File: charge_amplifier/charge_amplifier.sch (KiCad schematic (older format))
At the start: 31 parts, among them J1 TEST_1P, J2 TEST_1P, J3 Conn_01x02, J4 Conn_01x02, J5 Conn_01x02, J6 TEST_1P, U1 TL072

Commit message: Initial draft of layout
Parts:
- AE1: footprint (none) -> lib_fp:BNC_5227677-1
- D1: footprint (none) -> Diodes_SMD:D_SOD-323
- J1, J2, J6: footprint (none) -> Measurement_Points:Measurement_Point_Round-SMD-Pad_Small
- NE1: footprint (none) -> lib_fp:A1D-T
- U1: footprint (none) -> SMD_Packages:SOIC-8-N
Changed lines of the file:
@@
 LIBS:contrib
 LIBS:valves
+LIBS:charge_amplifier-cache
 EELAYER 25 0
 EELAYER END
@@
 F 0 "AE1" H 1575 3575 50  0000 R CNN
 F 1 "Antenna_Shield" H 1575 3500 50  0001 R CNN
-F 2 "" H 1650 3500 50  0001 C CNN
+F 2 "lib_fp:BNC_5227677-1" H 1650 3500 50  0001 C CNN
 F 3 "" H 1650 3500 50  0001 C CNN
 	1    1650 3400
@@
 F 0 "NE1" H 1775 3975 50  0000 L CNN
 F 1 "Lamp_Neon" H 2000 3950 50  0001 L CNN
-F 2 "" V 1975 4200 50  0001 C CNN
+F 2 "lib_fp:A1D-T" V 1975 4200 50  0001 C CNN
 F 3 "" V 1975 4200 50  0001 C CNN
 F 4 "Visual Communications Company - VCC" H 1975 4100 60  0001 C CNN "MFG Name"
@@
 F 0 "U1" H 4750 3950 50  0000 L CNN
 F 1 "TL072" H 4750 3550 50  0000 L CNN
-F 2 "" H 4750 3750 50  0001 C CNN
+F 2 "SMD_Packages:SOIC-8-N" H 4750 3750 50  0001 C CNN
 F 3 "" H 4750 3750 50  0001 C CNN
 F 4 "Texas Instruments" H 4750 3750 60  0001 C CNN "MFG Name"
@@
 F 0 "U1" H 7600 3925 50  0000 L CNN
 F 1 "TL072" H 7600 3525 50  0000 L CNN
-F 2 "" H 7600 3725 50  0001 C CNN
+F 2 "SMD_Packages:SOIC-8-N" H 7600 3725 50  0001 C CNN
 F 3 "" H 7600 3725 50  0001 C CNN
 F 4 "Value" H 7600 3725 60  0001 C CNN "MFG Name"
@@
 F 0 "J1" H 3750 4120 50  0000 C CNN
 F 1 "TEST_1P" H 3750 4050 50  0000 C CNN
-F 2 "" H 3950 3850 50  0001 C CNN
+F 2 "Measurement_Points:Measurement_Point_Round-SMD-Pad_Small" H 3950 3850 50  0001 C CNN
 F 3 "" H 3950 3850 50  0001 C CNN
 	1    3750 3850
@@
 F 0 "J2" H 5725 3970 50  0000 C CNN
 F 1 "TEST_1P" H 5725 3900 50  0000 C CNN
-F 2 "" H 5925 3700 50  0001 C CNN
+F 2 "Measurement_Points:Measurement_Point_Round-SMD-Pad_Small" H 5925 3700 50  0001 C CNN
 F 3 "" H 5925 3700 50  0001 C CNN
 	1    5725 3700
@@
 F 0 "J6" H 8225 3970 50  0000 C CNN
 F 1 "TEST_1P" H 8225 3900 50  0000 C CNN
-F 2 "" H 8425 3700 50  0001 C CNN
+F 2 "Measurement_Points:Measurement_Point_Round-SMD-Pad_Small" H 8425 3700 50  0001 C CNN
 F 3 "" H 8425 3700 50  0001 C CNN
 	1    8225 3700
@@
 F 0 "D1" H 2525 4225 50  0000 C CNN
 F 1 "D_Schottky" H 2525 4025 50  0001 C CNN
-F 2 "" H 2525 4125 50  0001 C CNN
+F 2 "Diodes_SMD:D_SOD-323" H 2525 4125 50  0001 C CNN
 F 3 "" H 2525 4125 50  0001 C CNN
 	1    2525 4125

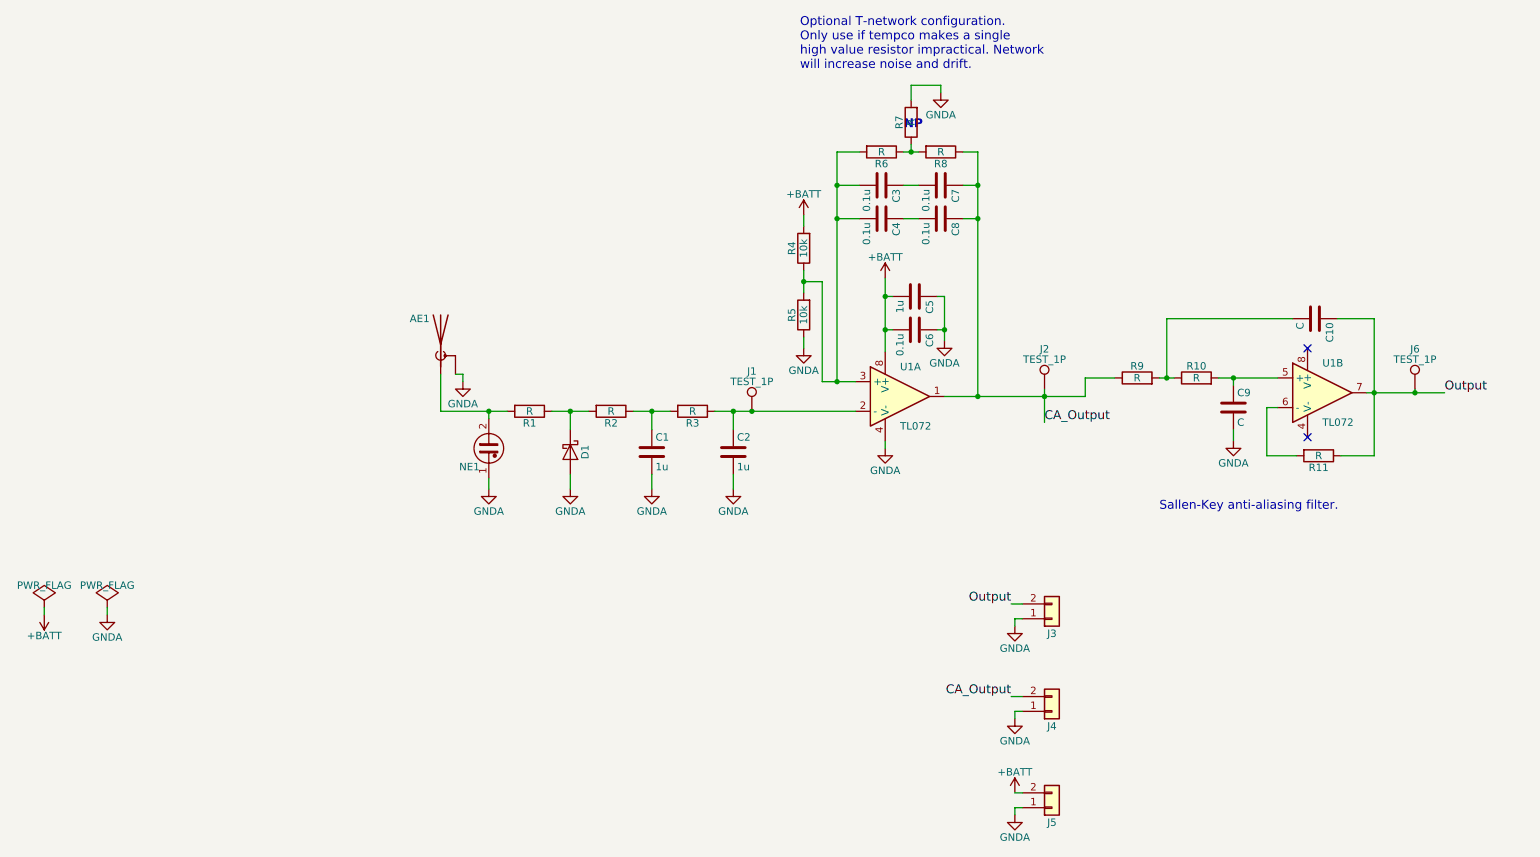
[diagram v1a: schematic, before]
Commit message: Fix schematic with bodges on Rev.A
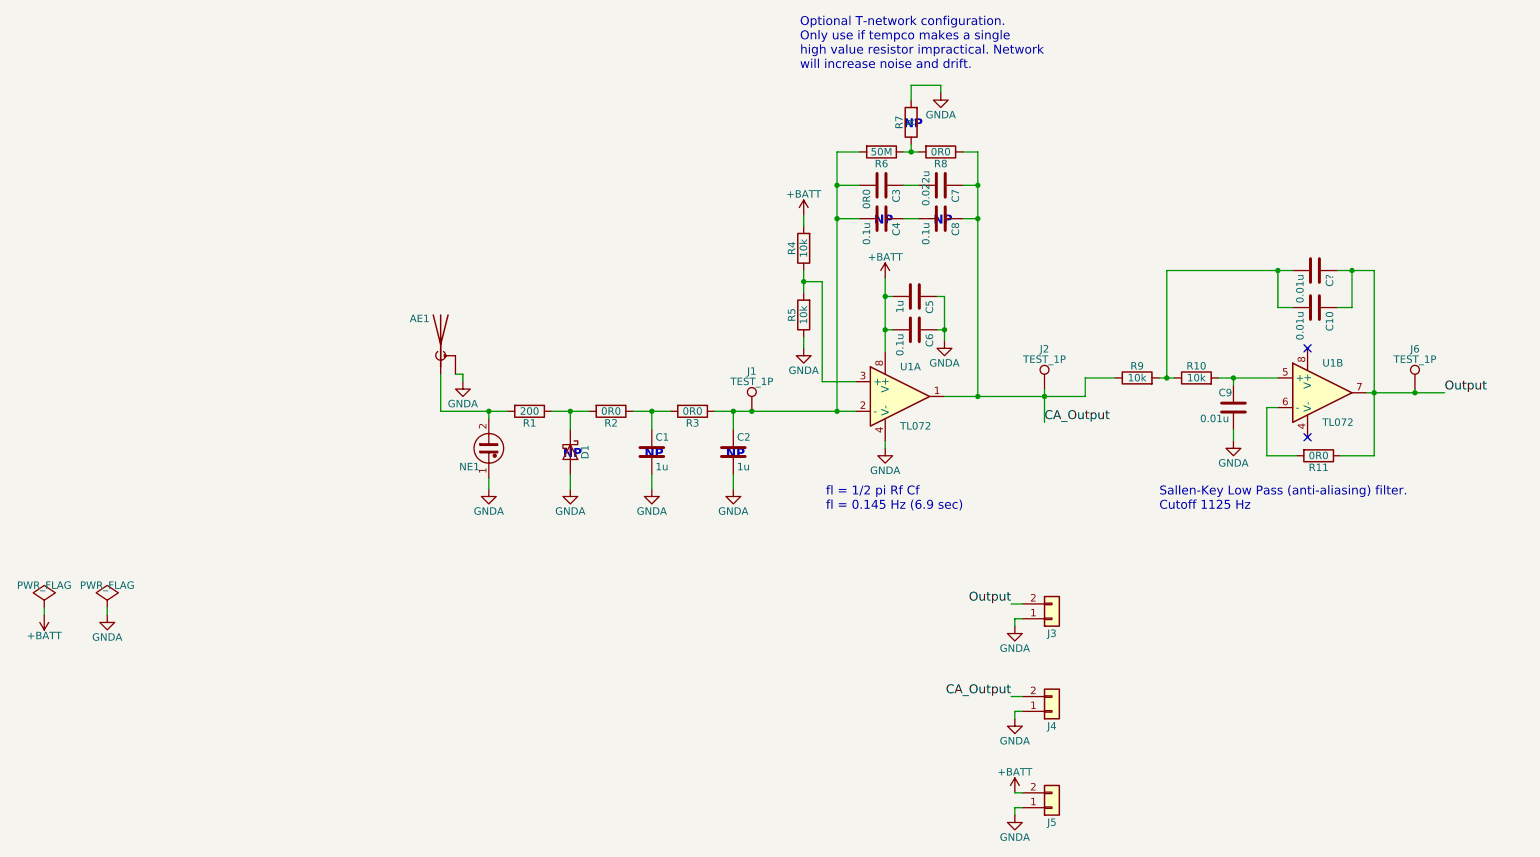
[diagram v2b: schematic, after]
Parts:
- added C?: 0.01u, Capacitors_SMD:C_0603_HandSoldering, symbol C
- C10, C9: value C -> 0.01u
- C3: value 0.1u -> 0R0
- C7: value 0.1u -> 0.022u
- R1: value R -> 200; 1st Distrib Link (none) -> Value; 1st Distrib PN (none) -> Value; 2nd Distrib Link (none) -> Value; 2nd Distrib PN (none) -> Value; MFG Name (none) -> Value; MFG Part Num (none) -> Value
- R10, R9: value R -> 10k
- R11, R2, R3, R8: value R -> 0R0; 1st Distrib Link (none) -> Value; 1st Distrib PN (none) -> Value; 2nd Distrib Link (none) -> Value; 2nd Distrib PN (none) -> Value; MFG Name (none) -> Value; MFG Part Num (none) -> Value
- R6: value R -> 50M; 1st Distrib Link (none) -> Value; 1st Distrib PN (none) -> Value; 2nd Distrib Link (none) -> Value; 2nd Distrib PN (none) -> Value; MFG Name (none) -> Value; MFG Part Num (none) -> Value
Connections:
- net Output: now also C?.1
- net at C2.1, J1.1, R3.1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: now also C3.2, C4.2, R6.2
- net at R4.1, R5.2, U1.3 (+): no longer C3.2, C4.2, R6.2
- net at C10.2, R10.1, R9.2: now also C?.2
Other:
- note added: "Sallen-Key Low Pass (anti-aliasing) filter.\nCutoff 1125 Hz"
- note added: "fl = 1/2 pi Rf Cf\nfl = 0.145 Hz (6.9 sec)"
- note removed: "Sallen-Key anti-aliasing filter."
- moved on the sheet: C10
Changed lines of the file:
@@
 P 2250 3850
 F 0 "R1" V 2330 3850 50  0000 C CNN
-F 1 "R" V 2250 3850 50  0000 C CNN
+F 1 "200" V 2250 3850 50  0000 C CNN
 F 2 "Resistors_SMD:R_0603_HandSoldering" V 2180 3850 50  0001 C CNN
 F 3 "" H 2250 3850 50  0001 C CNN
+F 4 "Value" H 2250 3850 60  0001 C CNN "MFG Name"
+F 5 "Value" H 2250 3850 60  0001 C CNN "MFG Part Num"
+F 6 "Value" H 2250 3850 60  0001 C CNN "1st Distrib PN"
+F 7 "Value" H 2250 3850 60  0001 C CNN "1st Distrib Link"
+F 8 "Value" H 2250 3850 60  0001 C CNN "2nd Distrib PN"
+F 9 "Value" H 2250 3850 60  0001 C CNN "2nd Distrib Link"
 	1    2250 3850
 	0    1    1    0
@@
 P 2800 3850
 F 0 "R2" V 2880 3850 50  0000 C CNN
-F 1 "R" V 2800 3850 50  0000 C CNN
+F 1 "0R0" V 2800 3850 50  0000 C CNN
 F 2 "Resistors_SMD:R_0603_HandSoldering" V 2730 3850 50  0001 C CNN
 F 3 "" H 2800 3850 50  0001 C CNN
+F 4 "Value" H 2800 3850 60  0001 C CNN "MFG Name"
+F 5 "Value" H 2800 3850 60  0001 C CNN "MFG Part Num"
+F 6 "Value" H 2800 3850 60  0001 C CNN "1st Distrib PN"
+F 7 "Value" H 2800 3850 60  0001 C CNN "1st Distrib Link"
+F 8 "Value" H 2800 3850 60  0001 C CNN "2nd Distrib PN"
+F 9 "Value" H 2800 3850 60  0001 C CNN "2nd Distrib Link"
 	1    2800 3850
 	0    1    1    0
@@
 P 3350 3850
 F 0 "R3" V 3430 3850 50  0000 C CNN
-F 1 "R" V 3350 3850 50  0000 C CNN
+F 1 "0R0" V 3350 3850 50  0000 C CNN
 F 2 "Resistors_SMD:R_0603_HandSoldering" V 3280 3850 50  0001 C CNN
 F 3 "" H 3350 3850 50  0001 C CNN
+F 4 "Value" H 3350 3850 60  0001 C CNN "MFG Name"
+F 5 "Value" H 3350 3850 60  0001 C CNN "MFG Part Num"
+F 6 "Value" H 3350 3850 60  0001 C CNN "1st Distrib PN"
+F 7 "Value" H 3350 3850 60  0001 C CNN "1st Distrib Link"
+F 8 "Value" H 3350 3850 60  0001 C CNN "2nd Distrib PN"
+F 9 "Value" H 3350 3850 60  0001 C CNN "2nd Distrib Link"
 	1    3350 3850
 	0    1    1    0
@@
 P 6350 3625
 F 0 "R9" V 6430 3625 50  0000 C CNN
-F 1 "R" V 6350 3625 50  0000 C CNN
+F 1 "10k" V 6350 3625 50  0000 C CNN
 F 2 "Resistors_SMD:R_0603_HandSoldering" V 6280 3625 50  0001 C CNN
 F 3 "" H 6350 3625 50  0001 C CNN
@@
 P 5025 2325
 F 0 "C7" H 5050 2425 50  0000 L CNN
-F 1 "0.1u" H 5050 2225 50  0000 L CNN
+F 1 "0.022u" H 4925 2225 50  0000 L CNN
 F 2 "Capacitors_SMD:C_0603_HandSoldering" H 5063 2175 50  0001 C CNN
 F 3 "" H 5025 2325 50  0001 C CNN
@@
 P 4625 2325
 F 0 "C3" H 4650 2425 50  0000 L CNN
-F 1 "0.1u" H 4650 2225 50  0000 L CNN
+F 1 "0R0" H 4650 2225 50  0000 L CNN
 F 2 "Capacitors_SMD:C_0603_HandSoldering" H 4663 2175 50  0001 C CNN
 F 3 "" H 4625 2325 50  0001 C CNN
@@
 P 4625 2100
 F 0 "R6" V 4705 2100 50  0000 C CNN
-F 1 "R" V 4625 2100 50  0000 C CNN
+F 1 "50M" V 4625 2100 50  0000 C CNN
 F 2 "Resistors_SMD:R_0603_HandSoldering" V 4555 2100 50  0001 C CNN
 F 3 "" H 4625 2100 50  0001 C CNN
+F 4 "Value" H 4625 2100 60  0001 C CNN "MFG Name"
+F 5 "Value" H 4625 2100 60  0001 C CNN "MFG Part Num"
+F 6 "Value" H 4625 2100 60  0001 C CNN "1st Distrib PN"
+F 7 "Value" H 4625 2100 60  0001 C CNN "1st Distrib Link"
+F 8 "Value" H 4625 2100 60  0001 C CNN "2nd Distrib PN"
+F 9 "Value" H 4625 2100 60  0001 C CNN "2nd Distrib Link"
 	1    4625 2100
 	0    1    1    0
@@
 P 5025 2100
 F 0 "R8" V 5105 2100 50  0000 C CNN
-F 1 "R" V 5025 2100 50  0000 C CNN
+F 1 "0R0" V 5025 2100 50  0000 C CNN
 F 2 "Resistors_SMD:R_0603_HandSoldering" V 4955 2100 50  0001 C CNN
 F 3 "" H 5025 2100 50  0001 C CNN
+F 4 "Value" H 5025 2100 60  0001 C CNN "MFG Name"
+F 5 "Value" H 5025 2100 60  0001 C CNN "MFG Part Num"
+F 6 "Value" H 5025 2100 60  0001 C CNN "1st Distrib PN"
+F 7 "Value" H 5025 2100 60  0001 C CNN "1st Distrib Link"
+F 8 "Value" H 5025 2100 60  0001 C CNN "2nd Distrib PN"
+F 9 "Value" H 5025 2100 60  0001 C CNN "2nd Distrib Link"
 	1    5025 2100
 	0    1    1    0
@@
 P 7575 4150
 F 0 "R11" V 7655 4150 50  0000 C CNN
-F 1 "R" V 7575 4150 50  0000 C CNN
+F 1 "0R0" V 7575 4150 50  0000 C CNN
 F 2 "Resistors_SMD:R_0603_HandSoldering" V 7505 4150 50  0001 C CNN
 F 3 "" H 7575 4150 50  0001 C CNN
+F 4 "Value" H 7575 4150 60  0001 C CNN "MFG Name"
+F 5 "Value" H 7575 4150 60  0001 C CNN "MFG Part Num"
+F 6 "Value" H 7575 4150 60  0001 C CNN "1st Distrib PN"
+F 7 "Value" H 7575 4150 60  0001 C CNN "1st Distrib Link"
+F 8 "Value" H 7575 4150 60  0001 C CNN "2nd Distrib PN"
+F 9 "Value" H 7575 4150 60  0001 C CNN "2nd Distrib Link"
 	1    7575 4150
 	0    1    1    0
@@
 Optional T-network configuration.\nOnly use if tempco makes a single\nhigh value resistor impractical. Network\nwill increase noise and drift.
 Text Notes 6500 4525 0    60   ~ 0
-Sallen-Key anti-aliasing filter.
+Sallen-Key Low Pass (anti-aliasing) filter.\nCutoff 1125 Hz
 $Comp
 L GNDA #PWR02
@@
 	4475 2100 4325 2100
 Wire Wire Line
-	4325 2100 4325 3650
-Connection ~ 4325 3650
-Wire Wire Line
 	4475 2325 4325 2325
 Connection ~ 4325 2325
@@
 	4875 2550 4775 2550
 Wire Wire Line
-	4475 2550 4325 2550
+	4325 2550 4475 2550
 Connection ~ 4325 2550
 Wire Wire Line
@@
 P 6750 3625
 F 0 "R10" V 6830 3625 50  0000 C CNN
-F 1 "R" V 6750 3625 50  0000 C CNN
+F 1 "10k" V 6750 3625 50  0000 C CNN
 F 2 "Resistors_SMD:R_0603_HandSoldering" V 6680 3625 50  0001 C CNN
 F 3 "" H 6750 3625 50  0001 C CNN
@@
 U 1 1 5A16ED57
 P 7000 3825
-F 0 "C9" H 7025 3925 50  0000 L CNN
-F 1 "C" H 7025 3725 50  0000 L CNN
+F 0 "C9" H 6900 3925 50  0000 L CNN
+F 1 "0.01u" H 6775 3750 50  0000 L CNN
 F 2 "Capacitors_SMD:C_0603_HandSoldering" H 7038 3675 50  0001 C CNN
 F 3 "" H 7000 3825 50  0001 C CNN
@@
 	7950 4150 7725 4150
 Wire Wire Line
-	7950 3225 7950 4150
+	7950 2900 7950 4150
 Connection ~ 7950 3725
 Wire Wire Line
@@
 L C C10
 U 1 1 5A16FAA0
-P 7550 3225
-F 0 "C10" H 7575 3325 50  0000 L CNN
-F 1 "C" H 7575 3125 50  0000 L CNN
-F 2 "Capacitors_SMD:C_0603_HandSoldering" H 7588 3075 50  0001 C CNN
-F 3 "" H 7550 3225 50  0001 C CNN
-F 4 "Value" H 7550 3225 60  0001 C CNN "MFG Name"
-F 5 "Value" H 7550 3225 60  0001 C CNN "MFG Part Num"
-F 6 "Value" H 7550 3225 60  0001 C CNN "1st Distrib PN"
-F 7 "Value" H 7550 3225 60  0001 C CNN "1st Distrib Link"
-F 8 "Value" H 7550 3225 60  0001 C CNN "2nd Distrib PN"
-F 9 "Value" H 7550 3225 60  0001 C CNN "2nd Distrib Link"
-	1    7550 3225
-	0    1    1    0
-$EndComp
-Wire Wire Line
-	6550 3625 6550 3225
-Wire Wire Line
-	6550 3225 7400 3225
+P 7550 3150
+F 0 "C10" H 7575 3250 50  0000 L CNN
+F 1 "0.01u" H 7575 3050 50  0000 L CNN
+F 2 "Capacitors_SMD:C_0603_HandSoldering" H 7588 3000 50  0001 C CNN
+F 3 "" H 7550 3150 50  0001 C CNN
+F 4 "Value" H 7550 3150 60  0001 C CNN "MFG Name"
+F 5 "Value" H 7550 3150 60  0001 C CNN "MFG Part Num"
+F 6 "Value" H 7550 3150 60  0001 C CNN "1st Distrib PN"
+F 7 "Value" H 7550 3150 60  0001 C CNN "1st Distrib Link"
+F 8 "Value" H 7550 3150 60  0001 C CNN "2nd Distrib PN"
+F 9 "Value" H 7550 3150 60  0001 C CNN "2nd Distrib Link"
+	1    7550 3150
+	0    1    1    0
+$EndComp
+Wire Wire Line
+	6550 2900 6550 3625
 Wire Wire Line
 	6500 3625 6600 3625
 Connection ~ 6550 3625
-Wire Wire Line
-	7700 3225 7950 3225
 $Comp
 L Conn_01x02 J5
@@
 Wire Wire Line
 	3075 3975 3075 3850
+$Comp
+L C C?
+U 1 1 5A2F632C
+P 7550 2900
+F 0 "C?" H 7575 3000 50  0000 L CNN
+F 1 "0.01u" H 7575 2800 50  0000 L CNN
+F 2 "Capacitors_SMD:C_0603_HandSoldering" H 7588 2750 50  0001 C CNN
+F 3 "" H 7550 2900 50  0001 C CNN
+F 4 "Value" H 7550 2900 60  0001 C CNN "MFG Name"
+F 5 "Value" H 7550 2900 60  0001 C CNN "MFG Part Num"
+F 6 "Value" H 7550 2900 60  0001 C CNN "1st Distrib PN"
+F 7 "Value" H 7550 2900 60  0001 C CNN "1st Distrib Link"
+F 8 "Value" H 7550 2900 60  0001 C CNN "2nd Distrib PN"
+F 9 "Value" H 7550 2900 60  0001 C CNN "2nd Distrib Link"
+	1    7550 2900
+	0    1    1    0
+$EndComp
+Wire Wire Line
+	6550 2900 7400 2900
+Wire Wire Line
+	7700 2900 7950 2900
+Wire Wire Line
+	7700 3150 7800 3150
+Wire Wire Line
+	7800 3150 7800 2900
+Connection ~ 7800 2900
+Wire Wire Line
+	7400 3150 7300 3150
+Wire Wire Line
+	7300 3150 7300 2900
+Connection ~ 7300 2900
+Text Notes 3025 4175 0    60   ~ 12
+NP
+Text Notes 4975 2600 0    60   ~ 12
+NP
+Text Notes 4575 2600 0    60   ~ 12
+NP
+Text Notes 3575 4175 0    60   ~ 12
+NP
+Text Notes 2475 4175 0    60   ~ 12
+NP
+Text Notes 4250 4525 0    60   ~ 0
+fl = 1/2 pi Rf Cf\nfl = 0.145 Hz (6.9 sec)
+Wire Wire Line
+	4325 2100 4325 3850
+Connection ~ 4325 3850
 $EndSCHEMATC
